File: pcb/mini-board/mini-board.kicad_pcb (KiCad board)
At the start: 2 copper layers, 100.3 x 99.7 mm, 44 parts, among them J1 USB_B, J2 EXPBUS1, J3 Serial, J6 UART1, SW1 RESET, SW2 NMI, SW3 SW_SPDT, U1 74AC14, U2 W65C02, U3 CD74HC688, U4 74AC10, U5 SST39SF040, U6 62256-55, U7 CD74HC688, U8 W65C51NxP, U9 MAX232, X1 14 MHz, Y1 1.8432 MHz

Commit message: Expanding README.md
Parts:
- removed C10, C11, C13, C14, C2, C5: 100nF, Capacitor_THT:C_Disc_D5.0mm_W2.5mm_P5.00mm
- removed C12: 30pF, Capacitor_THT:C_Disc_D5.0mm_W2.5mm_P5.00mm
- removed C15, C18, C19: 10uF, Capacitor_THT:CP_Radial_D5.0mm_P2.50mm
- removed C8: 100uF, Capacitor_THT:CP_Radial_D6.3mm_P2.50mm
- removed J6: UART1, Connector_Dsub:DSUB-9_Male_Horizontal_P2.77x2.84mm_EdgePinOffset4.94mm_Housed_MountingHolesOffset7.48mm
- removed R1, R4: 1k, Resistor_THT:R_Axial_DIN0207_L6.3mm_D2.5mm_P7.62mm_Horizontal
- removed R5: 100k, Resistor_THT:R_Axial_DIN0207_L6.3mm_D2.5mm_P7.62mm_Horizontal
- removed U1: 74AC14, Package_DIP:DIP-14_W7.62mm_Socket
- removed U3, U7: CD74HC688, Package_DIP:DIP-20_W7.62mm_Socket
- removed U4: 74AC10, Package_DIP:DIP-14_W7.62mm_Socket
- removed U5: SST39SF040, Package_DIP:DIP-32_W15.24mm_Socket
- removed U6: 62256-55, Package_DIP:DIP-28_W15.24mm_Socket
- removed U8: W65C51NxP, Package_DIP:DIP-28_W15.24mm_Socket
- removed U9: MAX232, Package_DIP:DIP-16_W7.62mm_Socket
- added C17: 100nF, Capacitor_THT:C_Disc_D5.0mm_W2.5mm_P5.00mm, F.Cu at (214.8, 99.1)
- added C24: 100nF, Capacitor_THT:C_Disc_D5.0mm_W2.5mm_P5.00mm, F.Cu at (186.4, 45.7)
- added C25: 30pF, Capacitor_THT:C_Disc_D5.0mm_W2.5mm_P5.00mm, F.Cu at (228.6, 54.4)
- added C26: 100nF, Capacitor_THT:C_Disc_D5.0mm_W2.5mm_P5.00mm, F.Cu at (243.8, 91.4)
- added C27: 100nF, Capacitor_THT:C_Disc_D5.0mm_W2.5mm_P5.00mm, F.Cu at (216.4, 45.7)
- added C28: 10uF, Capacitor_THT:CP_Radial_D5.0mm_P2.50mm, F.Cu at (203.2, 54.7)
- added C29: 10uF, Capacitor_THT:CP_Radial_D5.0mm_P2.50mm, F.Cu at (203.2, 62.4)
- added C30: 10uF, Capacitor_THT:CP_Radial_D5.0mm_P2.50mm, F.Cu at (203.2, 47.1)
- added C31: 10uF, Capacitor_THT:CP_Radial_D5.0mm_P2.50mm, F.Cu at (203.2, 70.0)
- added C33: 100nF, Capacitor_THT:C_Disc_D5.0mm_W2.5mm_P5.00mm, F.Cu at (185.4, 137.7)
- added C34: 100nF, Capacitor_THT:C_Disc_D5.0mm_W2.5mm_P5.00mm, F.Cu at (197.6, 120.4)
- added C35: 100nF, Capacitor_THT:C_Disc_D5.0mm_W2.5mm_P5.00mm, F.Cu at (180.4, 109.2)
- added C36: 100nF, Capacitor_THT:C_Disc_D5.0mm_W2.5mm_P5.00mm, F.Cu at (169.2, 125.4)
- added G002: OSHW-Logo2_7.3x6mm_SilkScreen, Symbol:OSHW-Logo2_7.3x6mm_SilkScreen, F.Cu at (226.1, 149.9)
- added H1: MountingHole, MountingHole:MountingHole_3.2mm_M3_DIN965_Pad_TopOnly, F.Cu at (130.6, 29.5)
- added H2: MountingHole, MountingHole:MountingHole_3.2mm_M3_DIN965_Pad_TopOnly, F.Cu at (255.5, 29.0)
- added H3: MountingHole, MountingHole:MountingHole_3.2mm_M3_DIN965_Pad_TopOnly, F.Cu at (255.5, 153.9)
- added H4: MountingHole, MountingHole:MountingHole_3.2mm_M3_DIN965_Pad_TopOnly, F.Cu at (130.6, 153.9)
- added J4: Atmel-JTAG-10, Connector_IDC:IDC-Header_2x05_P2.54mm_Vertical, F.Cu at (178.3, 148.6)
- added J5: Conn_02x18_Odd_Even, Connector_PinHeader_2.54mm:PinHeader_2x18_P2.54mm_Vertical, F.Cu at (133.3, 44.7)
- added J8: SERIAL, Connector_Dsub:DSUB-9_Pins_Horizontal_P2.77x2.84mm_EdgePinOffset4.94mm_Housed_MountingHolesOffset4.94mm, F.Cu at (198.6, 33.3)
- added R2: 100k, Resistor_THT:R_Axial_DIN0207_L6.3mm_D2.5mm_P7.62mm_Horizontal, F.Cu at (233.7, 46.7)
- added R9: 10k, Resistor_THT:R_Axial_DIN0207_L6.3mm_D2.5mm_P7.62mm_Horizontal, F.Cu at (143.5, 91.4)
- added U11: DS1813, Package_TO_SOT_THT:TO-92, F.Cu at (161.3, 152.4)
- added U15: SST39SF040, Package_DIP:DIP-32_W15.24mm_Socket, F.Cu at (233.7, 104.1)
- added U16: AS6C4008-55, Package_DIP:DIP-32_W15.24mm_Socket, F.Cu at (204.9, 104.1)
- added U19: W65C22NxP, Package_DIP:DIP-40_W15.24mm_Socket, F.Cu at (176.1, 50.8)
- added U21: W65C51NxP, Package_DIP:DIP-28_W15.24mm_Socket, F.Cu at (233.7, 52.7)
- added U22: MAX232, Package_DIP:DIP-16_W7.62mm_Socket, F.Cu at (210.1, 50.8)
- added U23: ATF1502AS, Package_LCC:PLCC-44_THT-Socket, F.Cu at (184.7, 116.8)
- C16: value 10uF -> 100nF; footprint Capacitor_THT:CP_Radial_D5.0mm_P2.50mm -> Capacitor_THT:C_Disc_D5.0mm_W2.5mm_P5.00mm
- C6: value 100nF -> 220uF; footprint Capacitor_THT:C_Disc_D5.0mm_W2.5mm_P5.00mm -> Capacitor_THT:CP_Radial_D6.3mm_P2.50mm
- C7: footprint Capacitor_THT:CP_Radial_D6.3mm_P2.50mm -> Capacitor_THT:CP_Radial_D5.0mm_P2.50mm
- J2: value EXPBUS1 -> Conn_02x14_Odd_Even; footprint Connector_PinHeader_2.54mm:PinHeader_2x20_P2.54mm_Vertical -> Connector_PinHeader_2.54mm:PinHeader_2x14_P2.54mm_Vertical
- J3: value Serial -> SD Card Board; footprint Connector_PinSocket_2.54mm:PinSocket_1x06_P2.54mm_Vertical -> sdcard-holder:sdcard-socket
- R6, R7: value 1k -> 10k
- SW1: value RESET -> SW_SPDT; footprint Button_Switch_THT:SW_PUSH_6mm -> components:power_switch
- SW2: value NMI -> RESET
- SW3: value SW_SPDT -> NMI; footprint components:power_switch -> Button_Switch_THT:SW_PUSH_6mm
- X1: value 14 MHz -> CLK
- moved C7 201.0 mm to (256.0, 57.4)
- moved J1 183.3 mm to (241.3, 40.6)
- moved R7 162.5 mm to (199.4, 154.9), turned to 90 degrees
- moved SW3 158.1 mm to (205.6, 149.9), turned to 0 degrees
- moved C9 149.6 mm to (217.2, 154.9), turned to 90 degrees
- moved SW1 147.8 mm to (223.6, 33.9), turned to 90 degrees
- moved C6 146.2 mm to (256.0, 46.7), turned to 180 degrees
- moved Y1 139.2 mm to (228.6, 71.5), turned to 90 degrees
- moved G001 138.2 mm to (239.8, 149.9)
- moved C16 130.4 mm to (243.8, 99.1), turned to 180 degrees
- moved R8 121.5 mm to (223.5, 65.4), turned to -90 degrees
- moved C3 103.4 mm to (210.9, 77.5), turned to 0 degrees
- moved U2 86.0 mm to (147.3, 83.8), turned to 0 degrees
- moved C1 84.0 mm to (166.4, 94.1), turned to -90 degrees
- moved X1 81.8 mm to (205.7, 90.2)
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- renumbered G*** to G001
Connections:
- C16 pad 1: Net-(U9-C2+) -> VCC
- C16 pad 2: Net-(U9-C2-) -> GND
- C6 pad 1: ~{NMI} -> VCC
- C9 pad 1: VCC -> ~{NMI}
- J2 pad 10: ~{RES} -> PA3
- J2 pad 11: A4 -> PB4
- J2 pad 12: ~{NMI} -> PA4
- J2 pad 13: A5 -> PB5
- J2 pad 14: ~{IRQC51_1} -> PA5
- J2 pad 15: A6 -> PB6
- J2 pad 16: unconnected-(J2-Pin_16-Pad16) -> PA6
- J2 pad 17: A7 -> PB7
- J2 pad 18: ~{I/O} -> PA7
- J2 pad 19: A8 -> CB1
- J2 pad 20: unconnected-(J2-Pin_20-Pad20) -> CA1
- J2 pad 21: A9 -> CB2
- J2 pad 22: unconnected-(J2-Pin_22-Pad22) -> CA2
- J2 pad 23: A10 -> R/~{W}
- J2 pad 24: D0 -> ~{RES}
- J2 pad 25: A11 -> ~{NMI}
- J2 pad 26: D1 -> CLK
- J2 pad 27: A12 -> GND
- J2 pad 28: D2 -> GND
- J2 pad 3: A0 -> PB0
- J2 pad 4: R/~{W} -> MISO
- J2 pad 5: A1 -> PB1
- J2 pad 6: CLK -> MOSI
- J2 pad 7: A2 -> PB2
- J2 pad 8: unconnected-(J2-Pin_8-Pad8) -> PA2
- J2 pad 9: A3 -> PB3
- J3 pad 1: ~{RTS1} -> PA3
- J3 pad 2: TxD1 -> PA2
- J3 pad 3: RxD1 -> MOSI
- J3 pad 4: VCC -> MISO
- J3 pad 5: ~{CTS1} -> VCC
- R6 pad 1: ~{NMI} -> ~{IRQ}
- R7 pad 1: ~{IRQC51_1} -> ~{NMI}
- SW1 pad 1: GND -> VCC
- SW1 pad 2: ~{RES} -> VIN
- SW2 pad 2: ~{NMI} -> ~{RES}
- SW3 pad 1: VCC -> GND
- SW3 pad 2: VIN -> ~{NMI}
- U2 pad 4: ~{IRQC51_1} -> ~{IRQ}
- X1 pad 8: Net-(X1-OUT) -> CLK
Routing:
- net VCC: track 667.3 -> 1274.0 mm
- net GND: track 766.2 -> 1208.7 mm, vias 1 -> 3
- net D5: track 138.8 -> 334.7 mm, vias 0 -> 3
- net R/~{W}: track 85.1 -> 270.2 mm, vias 1 -> 2
- net D7: track 138.0 -> 312.6 mm
- net ~{IRQ}: track 0.00 -> 165.4 mm, vias 0 -> 1
- net D6: track 134.3 -> 290.5 mm, vias 0 -> 1
- net D0: track 155.8 -> 308.1 mm, vias 1 -> 3
- net D3: track 150.2 -> 287.9 mm, vias 2 -> 3
- net CA1: track 0.00 -> 137.5 mm, vias 0 -> 2
- net A1: track 120.5 -> 255.8 mm, vias 1 -> 2
- net A15: track 202.9 -> 67.7 mm, vias 1 -> 0
- net CA2: track 0.00 -> 134.8 mm, vias 0 -> 3
- net ~{I/O}: track 130.1 -> 0.00 mm, vias 1 -> 0
- net D4: track 175.1 -> 301.0 mm, vias 2 -> 4
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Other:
- board size 100.3 x 99.7 mm -> 132.1 x 132.1 mm
- board text added: "/MINI/"
- board text added: "OFF"
- board text added: "ON"
- board text added: "SDCARD"
- board text added: "Sources: https://github.com/ifilot/bytecradle-6502"
- board text added: "VCC A0 A1 A2 A3 A4 A5 A6 A7 A8 A9 A10 A11 A12 A13 A14 A15 GND"
- board text added: "VCC D0 D1 D2 D3 D4 D5 D6 D7 ~{RES} CLK ~{NMI} R/~{W} ~{IRQ} GND Tx Rx GND"
- board text added: "VCC PA0 PA1 PA2 PA3 PA4 PA5 PA6 PA7 CA1 CA2 ~{RES} CLK GND"
- board text added: "VCC PB0 PB1 PB2 PB3 PB4 PB5 PB6 PB7 CB1 CB2 R/~{W} ~{NMI} GND"
- board text removed: "GND"
- board text removed: "RxD←TxD"
- board text removed: "TxD→RxD"
- board text removed: "VCC"
- board text removed: "VCC A0 A1 A2 A3 A4 A5 A6 A7 A8 A9 A10 A11 A12 A13 A14 A15 X X GND"
- board text removed: "VCC R/~{W} CLK X ~{RES} ~{NMI} ~{IRQ} X ~{I/O} X X D0 D1 D2 D3 D4 D5 D6 D7 GND"
- board text removed: "~{CTS}"
- board text removed: "~{RTS}"

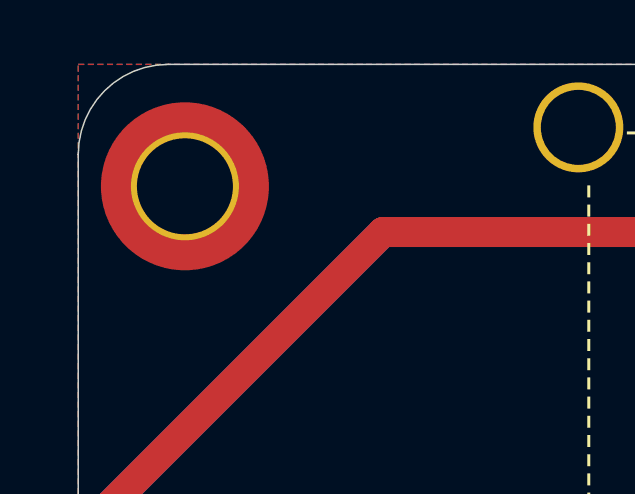
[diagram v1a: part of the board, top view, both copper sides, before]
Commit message: Fixing position hole
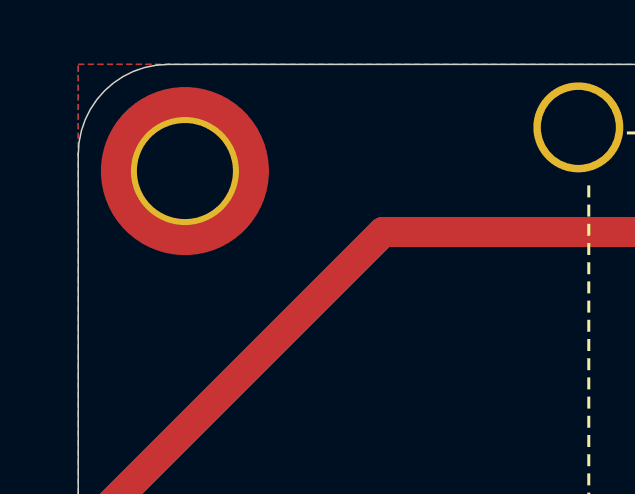
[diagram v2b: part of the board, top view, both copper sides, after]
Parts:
- moved H1 0.51 mm to (130.6, 29.0)
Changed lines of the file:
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@@
 	(footprint "MountingHole:MountingHole_3.2mm_M3_DIN965_Pad_TopOnly"
 		(layer "F.Cu")
-		(at 130.556 29.464)
+		(at 130.556 28.956)
 		(descr "Mounting Hole 3.2mm, M3, DIN965")
 		(tags "mounting hole 3.2mm m3 din965")

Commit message: Initial commit miniboard revision
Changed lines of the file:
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@@
 		(property "Value" "AS6C4008-55"
 			(at 7.62 40.43 0)
-			(layer "F.SilkS")
+			(layer "F.Fab")
 			(effects
 				(font
@@
 			)
 		)
+		(property "Sim.Pins" "1=K 2=A"
+			(at 0 0 0)
+			(unlocked yes)
+			(layer "F.Fab")
+			(hide yes)
+			(effects
+				(font
+					(size 1 1)
+					(thickness 0.15)
+				)
+			)
+		)
 		(property ki_fp_filters "LED* LED_SMD:* LED_THT:*")
 		(sheetname "/")
@@
 		(property "Value" "W65C22NxP"
 			(at 7.62 50.59 0)
-			(layer "F.SilkS")
+			(layer "F.Fab")
 			(effects
 				(font
@@
 		(property "Value" "W65C02"
 			(at 7.62 50.59 0)
-			(layer "F.SilkS")
+			(layer "F.Fab")
 			(effects
 				(font
@@
 		(property "Datasheet" "http://www.westerndesigncenter.com/wdc/documentation/w65c02s.pdf"
 			(at 0 0 0)
-			(unlocked yes)
 			(layer "F.Fab")
 			(hide yes)
@@
 		(property "Description" "8-bit CMOS General Purpose Microprocessor, DIP-40"
 			(at 0 0 0)
-			(unlocked yes)
 			(layer "F.Fab")
 			(hide yes)
@@
 		)
 		(fp_text user "${REFERENCE}"
-			(at 7.62 24.13 0)
+			(at 7.62 24.13 90)
 			(layer "F.Fab")
 			(effects
@@
 		(property "Value" "W65C51NxP"
 			(at 7.62 35.35 0)
-			(layer "F.SilkS")
+			(layer "F.Fab")
 			(effects
 				(font
@@
 			)
 		)
-		(property "Datasheet" " ~"
+		(property "Datasheet" ""
 			(at 0 0 90)
 			(unlocked yes)

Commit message: Pre-fourlayerboard commit
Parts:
- removed R6: 10k, Resistor_THT:R_Axial_DIN0207_L6.3mm_D2.5mm_P7.62mm_Horizontal
- added C4: 100nF, Capacitor_THT:C_Disc_D5.0mm_W2.5mm_P5.00mm, F.Cu at (161.5, 42.2)
- added R10: 10k, Resistor_THT:R_Axial_DIN0207_L6.3mm_D2.5mm_P7.62mm_Horizontal, F.Cu at (150.4, 27.4)
- added R11: 10k, Resistor_THT:R_Axial_DIN0207_L6.3mm_D2.5mm_P7.62mm_Horizontal, F.Cu at (153.9, 27.4)
- added R12: 10k, Resistor_THT:R_Axial_DIN0207_L6.3mm_D2.5mm_P7.62mm_Horizontal, F.Cu at (157.5, 27.4)
- added U1: 74AC11, Package_DIP:DIP-14_W7.62mm_Socket, F.Cu at (150.4, 42.2)
- J2: value Conn_02x14_Odd_Even -> EXPANSION BUS; footprint Connector_PinHeader_2.54mm:PinHeader_2x14_P2.54mm_Vertical -> Connector_PinHeader_2.54mm:PinHeader_2x20_P2.54mm_Vertical
- J5: value Conn_02x18_Odd_Even -> SYSTEM BUS; footprint Connector_PinHeader_2.54mm:PinHeader_2x18_P2.54mm_Vertical -> Connector_PinHeader_2.54mm:PinHeader_2x20_P2.54mm_Vertical
- moved J2 12.3 mm to (133.3, 97.5)
- moved J5 5.59 mm to (133.3, 39.1)
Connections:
- J2 pad 11: PB4 -> GND
- J2 pad 12: PA4 -> GND
- J2 pad 13: PB5 -> PB4
- J2 pad 14: PA5 -> PA4
- J2 pad 15: PB6 -> PB5
- J2 pad 16: PA6 -> PA5
- J2 pad 17: PB7 -> PB6
- J2 pad 18: PA7 -> PA6
- J2 pad 19: CB1 -> PB7
- J2 pad 20: CA1 -> PA7
- J2 pad 21: CB2 -> GND
- J2 pad 22: CA2 -> GND
- J2 pad 23: R/~{W} -> CB1
- J2 pad 24: ~{RES} -> CA1
- J2 pad 25: ~{NMI} -> CB2
- J2 pad 26: CLK -> CA2
- J2 pad 27: GND -> R/~{W}
- J2 pad 28: GND -> ~{RES}
- J5 pad 30: GND -> ~{IRQ0}
- J5 pad 32: TxD1 -> ~{IRQ1}
- J5 pad 34: RxD1 -> ~{IRQ2}
- J5 pad 35: GND -> ~{IRQ22}
- J5 pad 36: GND -> TxD1
- U19 pad 21: ~{IRQ} -> ~{IRQ22}
- U21 pad 26: ~{IRQ} -> ~{IRQ51}
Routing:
- net D5: track 334.7 -> 0.00 mm, vias 3 -> 0
- net D7: track 312.6 -> 0.00 mm, vias 2 -> 0
- net D0: track 308.1 -> 0.00 mm, vias 3 -> 0
- net D4: track 301.0 -> 0.00 mm, vias 4 -> 0
- net D1: track 290.7 -> 0.00 mm, vias 4 -> 0
- net D6: track 290.5 -> 0.00 mm, vias 1 -> 0
- net D3: track 287.9 -> 0.00 mm, vias 3 -> 0
- net A0: track 276.2 -> 0.00 mm, vias 2 -> 0
- net D2: track 273.0 -> 0.00 mm, vias 5 -> 0
- net R/~{W}: track 270.2 -> 0.00 mm, vias 2 -> 0
- net A1: track 255.8 -> 0.00 mm, vias 2 -> 0
- net ~{RES}: track 251.2 -> 0.00 mm, vias 3 -> 0
- net A2: track 241.3 -> 0.00 mm, vias 1 -> 0
- net A3: track 238.4 -> 0.00 mm, vias 2 -> 0
- net A4: track 203.9 -> 0.00 mm, vias 4 -> 0
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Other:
- board text added: "VCC A0 A1 A2 A3 A4 A5 A6 A7 A8 A9 A10 A11 A12 A13 A14 A15 ~{I22} ~{I51} GND"
- board text added: "VCC D0 D1 D2 D3 D4 D5 D6 D7 ~{RES} CLK ~{NMI} R/~{W} ~{IRQ} ~{IR0} ~{IR1} ~{IR2} Tx Rx GND"
- board text added: "VCC PA0 PA1 PA2 PA3 GND PA4 PA5 PA6 PA7 GND CA1 CA2 ~{RES} CLK GND Tx Rx VCC GND"
- board text added: "VCC PB0 PB1 PB2 PB3 GND PB4 PB5 PB6 PB7 GND CB1 CB2 R/~{W} ~{NMI} GND ~{VIA} ~{I22} VCC GND"
- board text removed: "VCC A0 A1 A2 A3 A4 A5 A6 A7 A8 A9 A10 A11 A12 A13 A14 A15 GND"
- board text removed: "VCC D0 D1 D2 D3 D4 D5 D6 D7 ~{RES} CLK ~{NMI} R/~{W} ~{IRQ} GND Tx Rx GND"
- board text removed: "VCC PA0 PA1 PA2 PA3 PA4 PA5 PA6 PA7 CA1 CA2 ~{RES} CLK GND"
- board text removed: "VCC PB0 PB1 PB2 PB3 PB4 PB5 PB6 PB7 CB1 CB2 R/~{W} ~{NMI} GND"

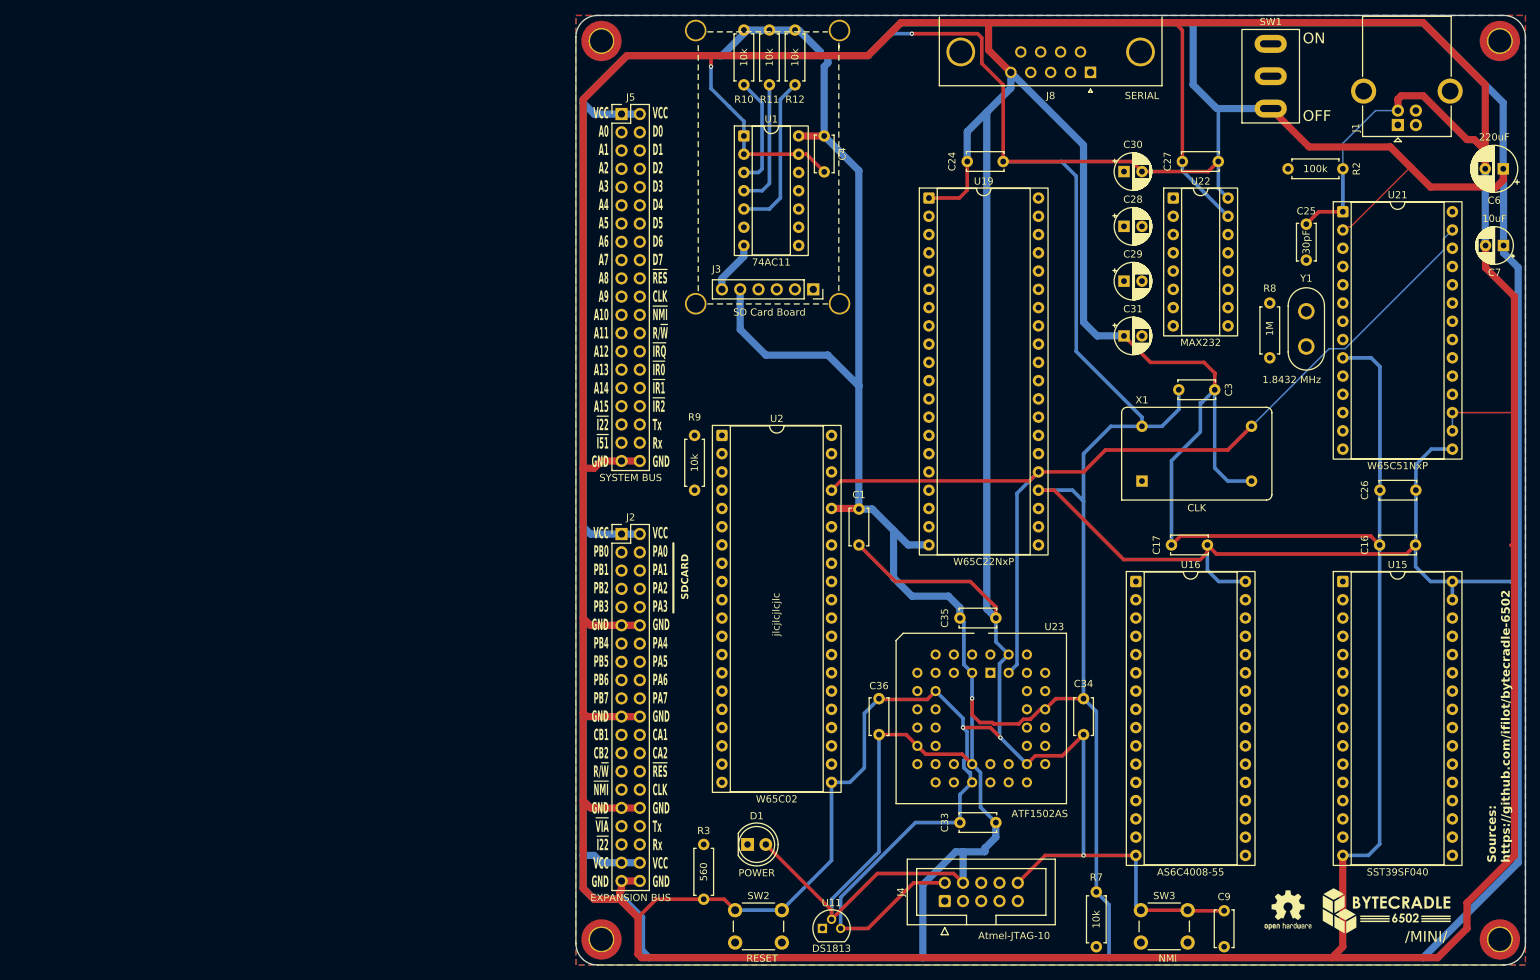
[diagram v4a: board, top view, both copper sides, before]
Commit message: Adding documentation to schematics
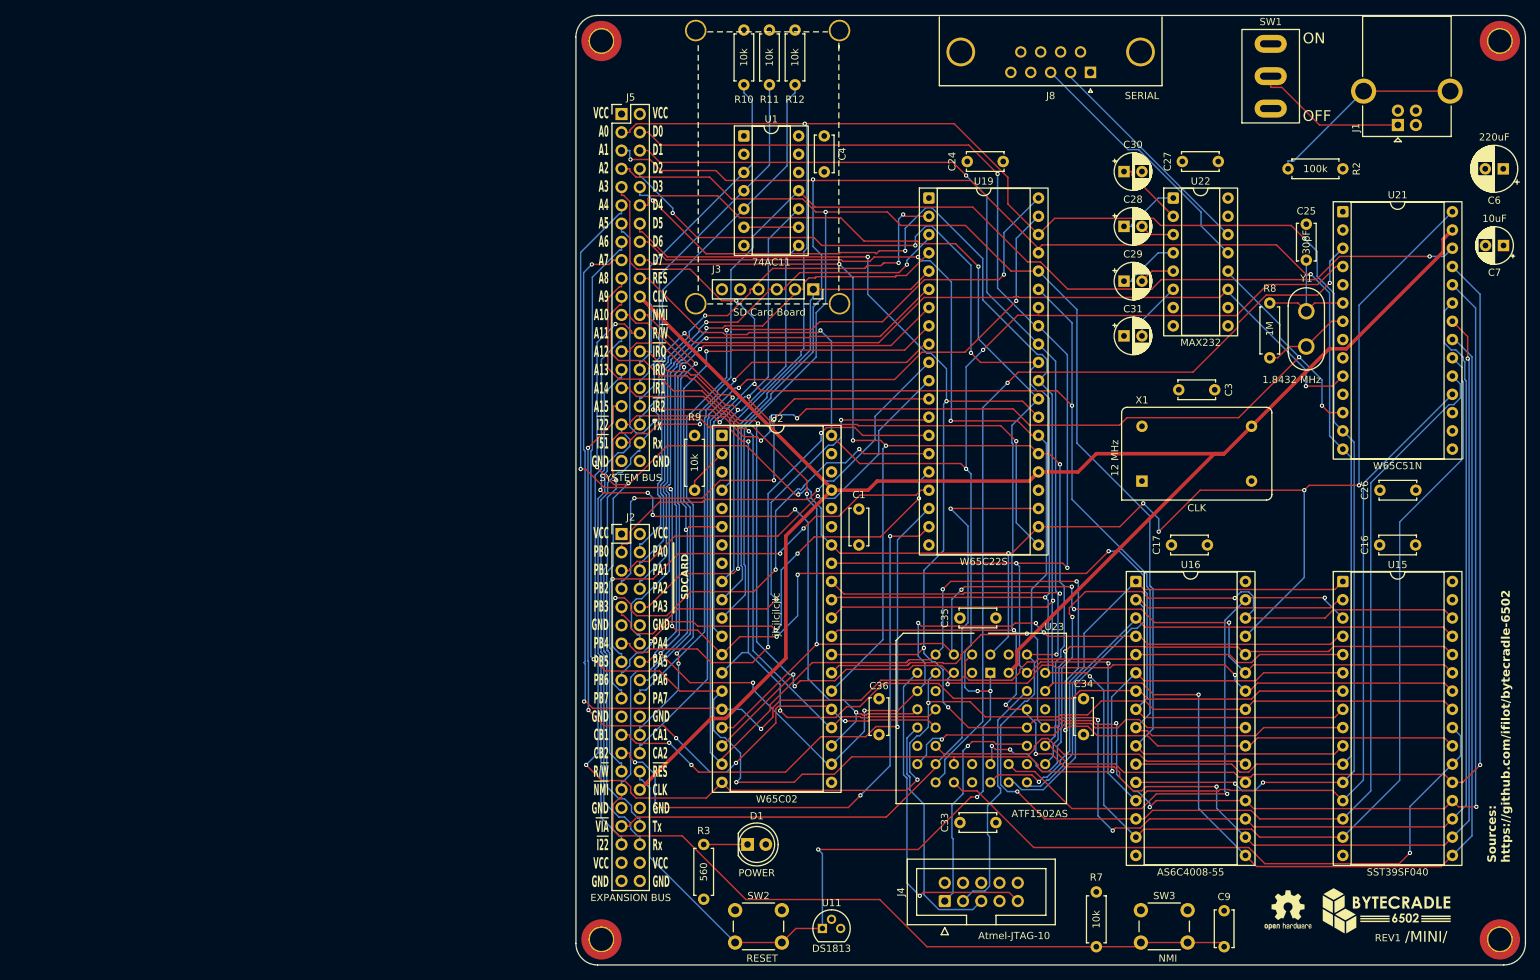
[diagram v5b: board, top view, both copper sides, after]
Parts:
- U19: value W65C22NxP -> W65C22S
- U21: value W65C51NxP -> W65C51N
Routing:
- net GND: track 1231.2 -> 30.0 mm, vias 4 -> 0
- net VCC: track 1227.5 -> 31.3 mm, vias 2 -> 0
- net D3: track 0.00 -> 309.5 mm, vias 0 -> 4
- net D6: track 0.00 -> 297.6 mm, vias 0 -> 6
- net D7: track 0.00 -> 296.8 mm, vias 0 -> 5
- net D1: track 0.00 -> 296.5 mm, vias 0 -> 4
- net D4: track 0.00 -> 294.8 mm, vias 0 -> 6
- net D5: track 0.00 -> 294.3 mm, vias 0 -> 6
- net D2: track 0.00 -> 288.7 mm, vias 0 -> 5
- net D0: track 0.00 -> 285.8 mm, vias 0 -> 4
- net A0: track 0.00 -> 283.9 mm, vias 0 -> 4
- net R/~{W}: track 0.00 -> 277.3 mm, vias 0 -> 9
- net A1: track 0.00 -> 270.3 mm, vias 0 -> 3
- net ~{RES}: track 0.00 -> 269.6 mm, vias 0 -> 7
- net A2: track 0.00 -> 230.3 mm, vias 0 -> 1
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- added copper zone on In1.Cu, net GND
- added copper zone on In2.Cu, net VCC
- removed copper zone on F.Cu, net GND
- removed copper zone on B.Cu, net VCC
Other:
- copper layers 2 -> 4
- board text added: "12 MHz"
- board text added: "REV1"

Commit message: Rivising board
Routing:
- net A5: track 174.8 -> 237.3 mm, vias 3 -> 1
- net GND: track 30.0 -> 65.5 mm
- net VCC: track 31.3 -> 65.3 mm
- net R/~{W}: track 277.3 -> 246.6 mm, vias 9 -> 3
- net A15: track 103.1 -> 73.3 mm, vias 5 -> 1
- net A10: track 216.7 -> 190.5 mm, vias 4 -> 2
- net CB2: track 83.8 -> 59.0 mm, vias 4 -> 1
- net A6: track 195.8 -> 176.0 mm, vias 3 -> 2
- net B4: track 97.3 -> 78.2 mm, vias 4 -> 2
- net D4: track 294.8 -> 313.8 mm, vias 6 -> 2
- net CB1: track 75.6 -> 58.3 mm, vias 3 -> 1
- net A13: track 96.5 -> 79.5 mm, vias 5 -> 1
- net PB4: track 71.5 -> 55.6 mm, vias 2 -> 1
- net PA6: track 83.7 -> 67.8 mm, vias 1 -> 0
- net PA4: track 82.8 -> 67.5 mm, vias 1 -> 0
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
